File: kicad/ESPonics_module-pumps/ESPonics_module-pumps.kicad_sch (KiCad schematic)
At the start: 7 parts, among them J1 RJ45, J2 Conn_01x02_Pin, J3 Conn_01x02_Pin, J4 Conn_01x01_Pin, J5 Conn_01x03_Pin, J6 Conn_01x07_Pin, J7 Conn_01x03_Pin

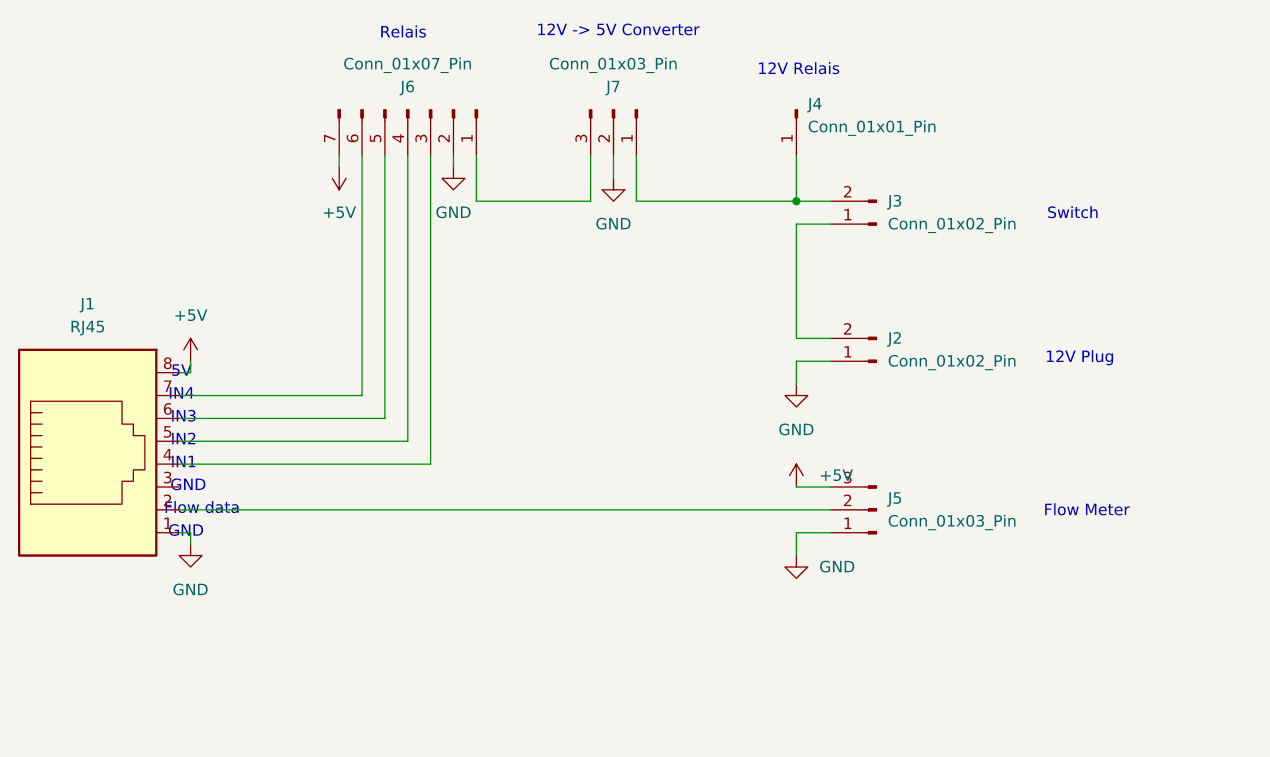
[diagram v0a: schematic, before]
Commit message: Add power converter to pump module schematic
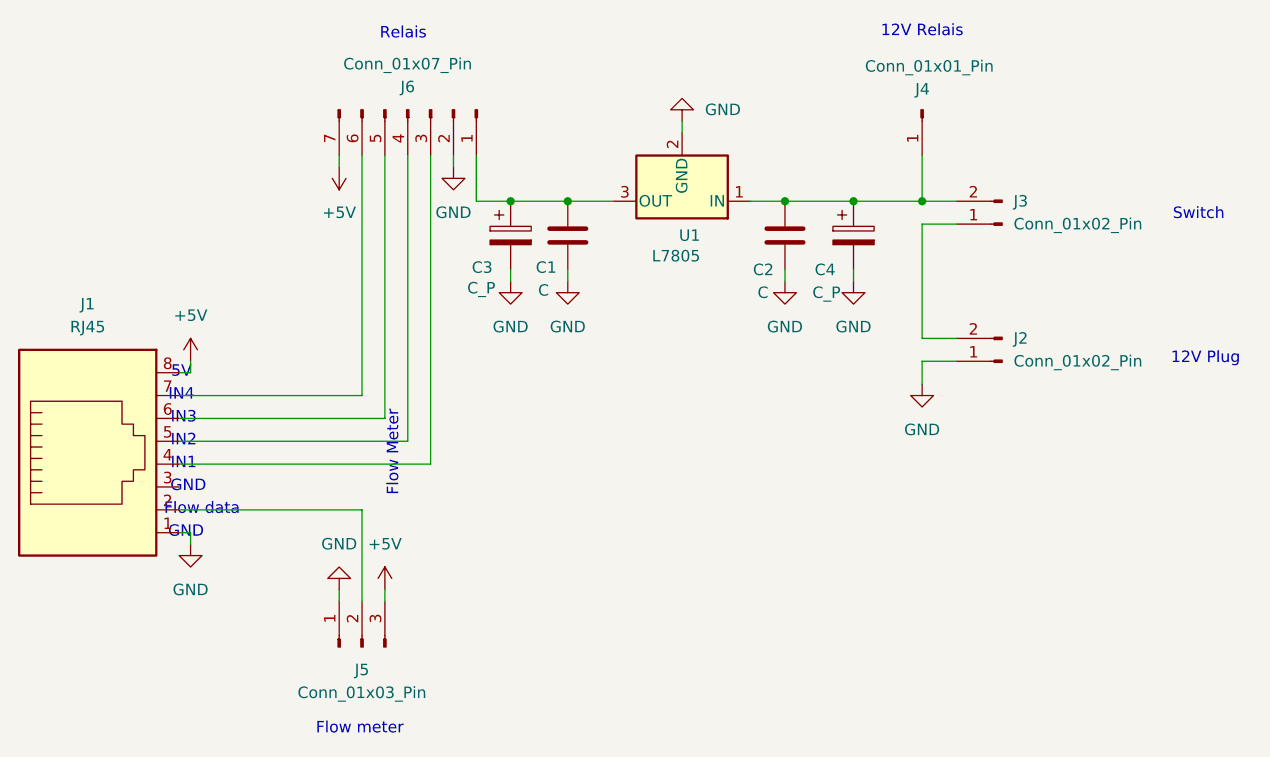
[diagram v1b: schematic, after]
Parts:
- removed J7: Conn_01x03_Pin, symbol Connector:Conn_01x03_Pin
- added C1, C2: C, symbol Device:C
- added C3, C4: C_P, symbol Device:C_Polarized
- added U1: L7805, symbol Regulator_Linear:L7805
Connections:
- net GND: now also C1.2, C2.2, C3.2, C4.2, U1.2 (GND)
- net at J3.2 (Pin_2), J4.1 (Pin_1): now also C2.1, C4.1, U1.1 (IN)
- net at J6.1 (Pin_1): now also C1.1, C3.1, U1.3 (OUT)
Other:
- note added: "Flow meter"
- note removed: "12V -> 5V Converter"
- moved on the sheet: J2, J3, J4

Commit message: Small changes to schematics
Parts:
- C1, C2: value C -> 100nF
- C3, C4: value C_P -> 10uF
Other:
- note removed: "Flow meter"
- moved on the sheet: J5
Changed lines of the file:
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@@
+	(wire
+		(pts
+			(xy 76.2 78.74) (xy 76.2 81.28)
+		)
+		(stroke
+			(width 0)
+			(type default)
+		)
+	)
 	(wire
 		(pts
@@
 	(wire
 		(pts
+			(xy 78.74 73.66) (xy 76.2 73.66)
+		)
+		(stroke
+			(width 0)
+			(type default)
+		)
+	)
+	(wire
+		(pts
 			(xy 54.61 53.34) (xy 54.61 52.07)
 		)
@@
 	(wire
 		(pts
+			(xy 73.66 76.2) (xy 78.74 76.2)
+		)
+		(stroke
+			(width 0)
+			(type default)
+		)
+	)
+	(wire
+		(pts
 			(xy 76.2 58.42) (xy 76.2 29.21)
 		)
@@
 	(wire
 		(pts
-			(xy 73.66 68.58) (xy 73.66 78.74)
-		)
-		(stroke
-			(width 0)
-			(type default)
-		)
-	)
-	(wire
-		(pts
-			(xy 76.2 77.47) (xy 76.2 78.74)
+			(xy 73.66 68.58) (xy 73.66 76.2)
 		)
 		(stroke
@@
 	(wire
 		(pts
+			(xy 76.2 73.66) (xy 76.2 71.12)
+		)
+		(stroke
+			(width 0)
+			(type default)
+		)
+	)
+	(wire
+		(pts
 			(xy 135.89 52.07) (xy 135.89 54.61)
 		)
@@
 	(wire
 		(pts
-			(xy 71.12 77.47) (xy 71.12 78.74)
+			(xy 78.74 78.74) (xy 76.2 78.74)
 		)
 		(stroke
@@
 	(wire
 		(pts
-			(xy 53.34 68.58) (xy 73.66 68.58)
-		)
-		(stroke
-			(width 0)
-			(type default)
-		)
-	)
-	(wire
-		(pts
 			(xy 90.17 41.91) (xy 90.17 43.18)
 		)
@@
 		(pts
 			(xy 139.7 52.07) (xy 135.89 52.07)
+		)
+		(stroke
+			(width 0)
+			(type default)
+		)
+	)
+	(wire
+		(pts
+			(xy 73.66 68.58) (xy 53.34 68.58)
 		)
 		(stroke
@@
 		)
 	)
-	(text "Flow meter"
-		(exclude_from_sim no)
-		(at 73.406 92.964 0)
-		(effects
-			(font
-				(size 1.27 1.27)
-			)
-		)
-	)
 	(text "Flow Meter"
 		(exclude_from_sim no)
-		(at 77.089 62.357 90)
+		(at 101.092 76.962 90)
 		(effects
 			(font
@@
 	(symbol
 		(lib_id "power:GND")
-		(at 71.12 77.47 180)
+		(at 76.2 81.28 0)
 		(unit 1)
 		(exclude_from_sim no)
@@
 		(fields_autoplaced yes)
 		(property "Reference" "#PWR07"
-			(at 71.12 71.12 0)
+			(at 76.2 87.63 0)
 			(effects
 				(font
@@
 		)
 		(property "Value" "GND"
-			(at 71.12 72.39 0)
+			(at 76.2 86.36 0)
 			(effects
 				(font
@@
 		)
 		(property "Footprint" ""
-			(at 71.12 77.47 0)
+			(at 76.2 81.28 0)
 			(effects
 				(font
@@
 		)
 		(property "Datasheet" ""
-			(at 71.12 77.47 0)
+			(at 76.2 81.28 0)
 			(effects
 				(font
@@
 		)
 		(property "Description" "Power symbol creates a global label with name \"GND\" , ground"
-			(at 71.12 77.47 0)
+			(at 76.2 81.28 0)
 			(effects
 				(font
@@
 		(dnp no)
 		(property "Reference" "C4"
-			(at 123.952 41.91 0)
+			(at 131.064 38.1 0)
 			(effects
 				(font
@@
 			)
 		)
-		(property "Value" "C_P"
-			(at 123.698 44.45 0)
+		(property "Value" "10uF"
+			(at 130.302 40.64 0)
 			(effects
 				(font
@@
 		(dnp no)
 		(property "Reference" "C1"
-			(at 92.964 41.656 0)
+			(at 99.314 38.1 0)
 			(effects
 				(font
@@
 			)
 		)
-		(property "Value" "C"
-			(at 93.218 44.196 0)
+		(property "Value" "100nF"
+			(at 97.79 40.64 0)
 			(effects
 				(font
@@
 		(dnp no)
 		(property "Reference" "C3"
-			(at 85.852 41.656 0)
+			(at 85.344 38.1 0)
 			(effects
 				(font
@@
 			)
 		)
-		(property "Value" "C_P"
-			(at 85.344 43.942 0)
+		(property "Value" "10uF"
+			(at 85.344 40.64 0)
 			(effects
 				(font
@@
 	(symbol
 		(lib_id "power:+5V")
-		(at 76.2 77.47 0)
+		(at 76.2 71.12 0)
 		(unit 1)
 		(exclude_from_sim no)
@@
 		(fields_autoplaced yes)
 		(property "Reference" "#PWR06"
-			(at 76.2 81.28 0)
+			(at 76.2 74.93 0)
 			(effects
 				(font
@@
 		)
 		(property "Value" "+5V"
-			(at 76.2 72.39 0)
+			(at 76.2 66.04 0)
 			(effects
 				(font
@@
 		)
 		(property "Footprint" ""
-			(at 76.2 77.47 0)
+			(at 76.2 71.12 0)
 			(effects
 				(font
@@
 		)
 		(property "Datasheet" ""
-			(at 76.2 77.47 0)
+			(at 76.2 71.12 0)
 			(effects
 				(font
@@
 		)
 		(property "Description" "Power symbol creates a global label with name \"+5V\""
-			(at 76.2 77.47 0)
+			(at 76.2 71.12 0)
 			(effects
 				(font
@@
 	(symbol
 		(lib_id "Connector:Conn_01x03_Pin")
-		(at 73.66 83.82 90)
+		(at 83.82 76.2 180)
 		(unit 1)
 		(exclude_from_sim no)
@@
 		(fields_autoplaced yes)
 		(property "Reference" "J5"
-			(at 73.66 86.36 90)
-			(effects
-				(font
-					(size 1.27 1.27)
-				)
+			(at 85.09 74.93 0)
+			(effects
+				(font
+					(size 1.27 1.27)
+				)
+				(justify right)
 			)
 		)
 		(property "Value" "Conn_01x03_Pin"
-			(at 73.66 88.9 90)
-			(effects
-				(font
-					(size 1.27 1.27)
-				)
+			(at 85.09 77.47 0)
+			(effects
+				(font
+					(size 1.27 1.27)
+				)
+				(justify right)
 			)
 		)
 		(property "Footprint" ""
-			(at 73.66 83.82 0)
+			(at 83.82 76.2 0)
 			(effects
 				(font
@@
 		)
 		(property "Datasheet" "~"
-			(at 73.66 83.82 0)
+			(at 83.82 76.2 0)
 			(effects
 				(font
@@
 		)
 		(property "Description" "Generic connector, single row, 01x03, script generated"
-			(at 73.66 83.82 0)
+			(at 83.82 76.2 0)
 			(effects
 				(font
@@
 		(dnp no)
 		(property "Reference" "C2"
-			(at 117.094 41.91 0)
+			(at 115.824 38.1 0)
 			(effects
 				(font
@@
 			)
 		)
-		(property "Value" "C"
-			(at 117.602 44.45 0)
-			(effects
-				(font
+		(property "Value" "100nF"
+			(at 114.808 40.64 0)
+			(effects
+				(font
